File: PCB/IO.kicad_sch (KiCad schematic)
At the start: 39 parts, among them J401 Conn_01x05_Pin, J402 USB_C_Receptacle_USB2.0_16P, J403 Screw_Terminal_01x06, J404 Screw_Terminal_01x04, J405 Conn_02x03_Counter_Clockwise, J406 Conn_02x03_Counter_Clockwise, J408 Conn_01x04, Q401 SL2302S, SW401 SW_Push, SW402 SW_Push

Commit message: Made changes discussed in the design review
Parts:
- removed TP401, TP402, TP403: TestPoint, TestPoint:TestPoint_Pad_D1.5mm, symbol Connector:TestPoint
- added J407: Conn_01x05_Pin, Connector_PinHeader_2.54mm:PinHeader_1x05_P2.54mm_Vertical, symbol Connector:Conn_01x05_Pin
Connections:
- net +3.3V: now also J407.1 (Pin_1)
- net GND: now also J407.5 (Pin_5)
- net GPIO1: now also J407.2 (Pin_2)
- net GPIO2: now also J407.3 (Pin_3)
- net GPIO3: now also J407.4 (Pin_4)
- net VIN renamed VBAT
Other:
- note added: "DFU/RST Button"
- note added: "GPIO"
- note removed: "DFU/RST Buttons"
- note removed: "GPIO Testpoints"
- moved on the sheet: SW401, SW402

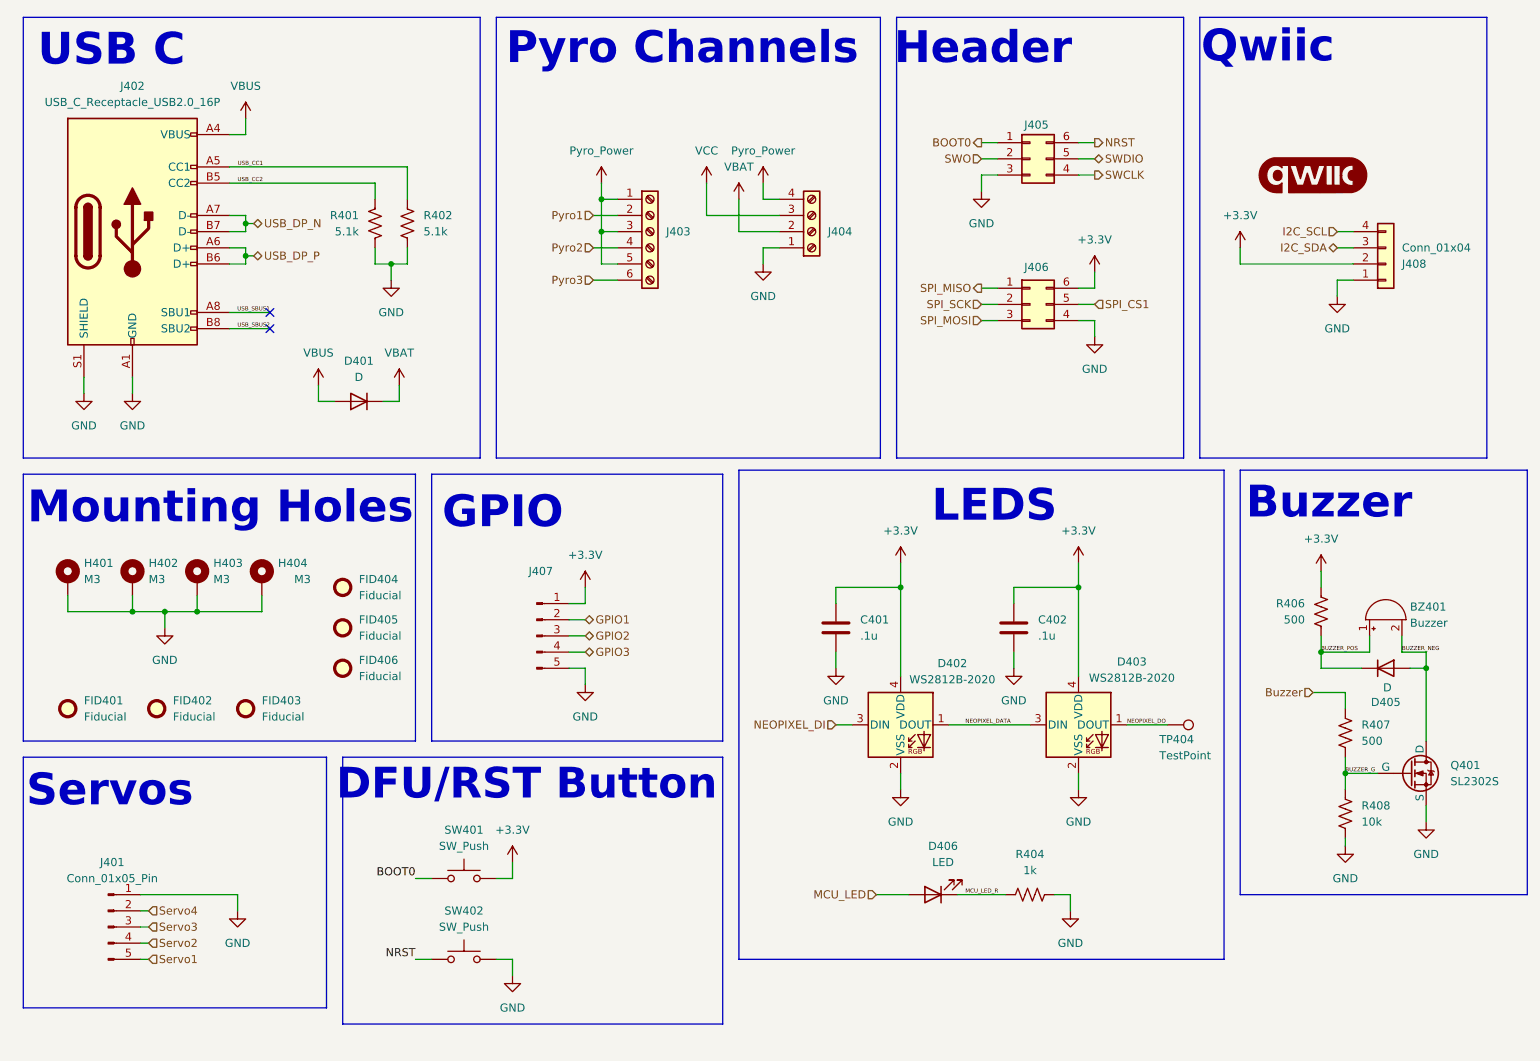
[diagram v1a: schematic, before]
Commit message: Added power pins to the programming header. Moved NeoPixels out location to the GPIO header Reran build job
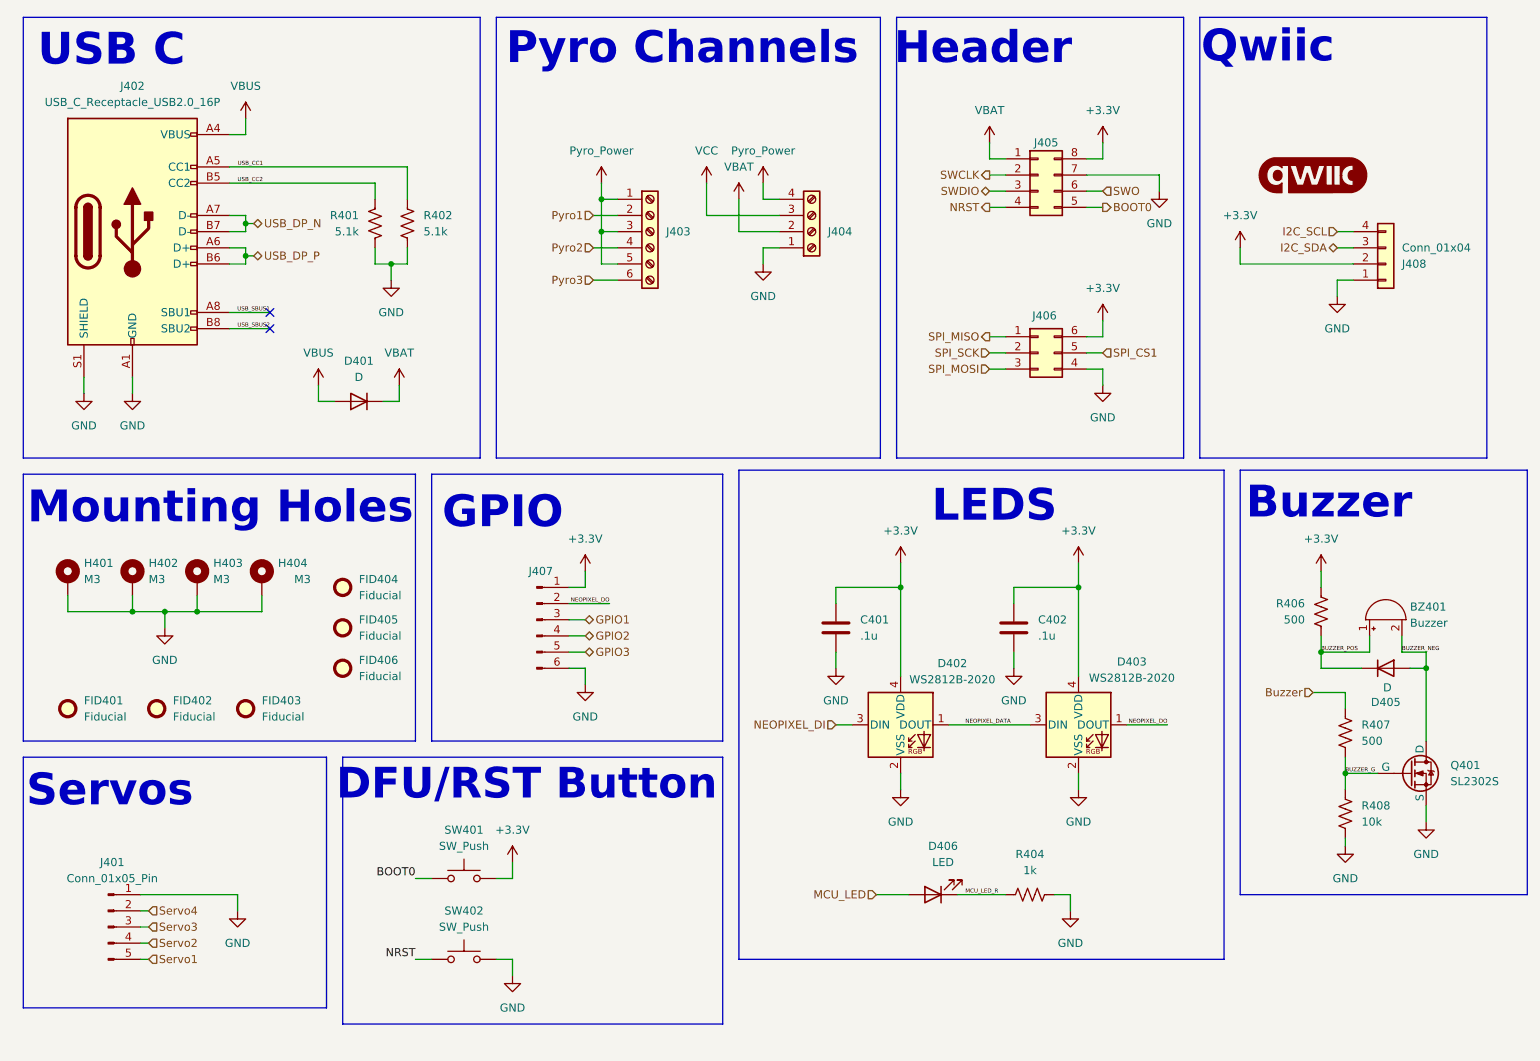
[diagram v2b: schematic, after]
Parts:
- removed J405: Conn_02x03_Counter_Clockwise, imported:EdgePinHeader_02x03, symbol Connector_Generic:Conn_02x03_Counter_Clockwise
- removed J407: Conn_01x05_Pin, Connector_PinHeader_2.54mm:PinHeader_1x05_P2.54mm_Vertical, symbol Connector:Conn_01x05_Pin
- removed TP404: TestPoint, TestPoint:TestPoint_Pad_D1.5mm, symbol Connector:TestPoint
- added J405: Conn_02x04_Counter_Clockwise, imported:EdgePinHeader_02x04, symbol Connector_Generic:Conn_02x04_Counter_Clockwise
- added J407: Conn_01x06_Pin, Connector_PinHeader_2.54mm:PinHeader_1x06_P2.54mm_Vertical, symbol Connector:Conn_01x06_Pin
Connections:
- net +3.3V: now also J405.8 (Pin_8), J407.1 (Pin_1)
- net BOOT0: now also J405.5 (Pin_5)
- net GND: now also J405.7 (Pin_7), J407.6 (Pin_6)
- net GPIO1: now also J407.3 (Pin_3)
- net GPIO2: now also J407.4 (Pin_4)
- net GPIO3: now also J407.5 (Pin_5)
- net NEOPIXEL_DO: now also J407.2 (Pin_2)
- net NRST: now also J405.4 (Pin_4)
- net SWCLK: now also J405.2 (Pin_2)
- net SWDIO: now also J405.3 (Pin_3)
- net SWO: now also J405.6 (Pin_6)
- net VBAT: now also J405.1 (Pin_1)
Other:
- moved on the sheet: J406
